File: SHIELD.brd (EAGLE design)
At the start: 67 x 61.7 mm, 12 parts

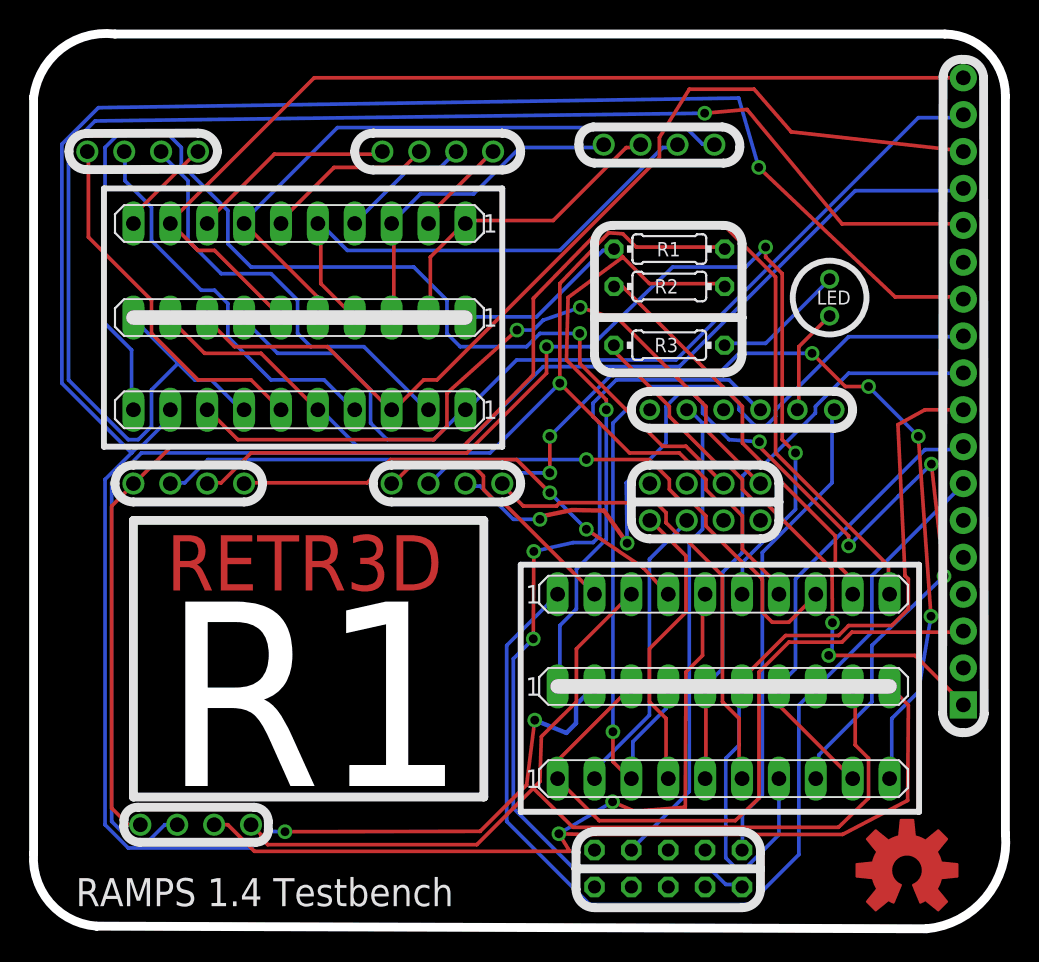
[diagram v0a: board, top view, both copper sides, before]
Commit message: Added images
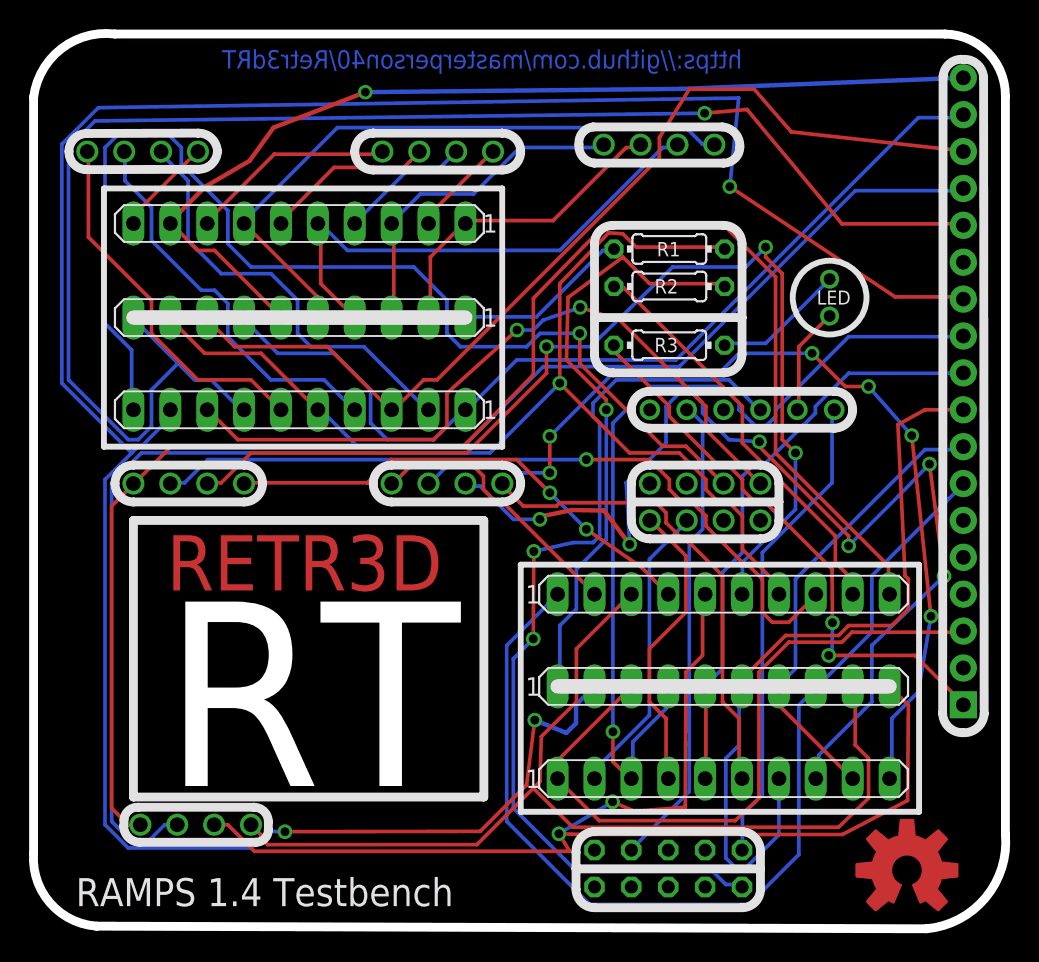
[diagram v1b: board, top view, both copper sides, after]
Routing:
- net N$36: track 166.8 -> 168.7 mm
- net N$27: track 69.1 -> 68.2 mm, vias 0 -> 1
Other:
- board text added: "RT"
- board text added: "https://github.com/masterperson40/Retr3dRT"
- board text removed: "R1"
